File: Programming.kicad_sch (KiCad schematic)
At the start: 4 parts, among them J1 Programming Header, J2 Programming Jumper, SW4 EN

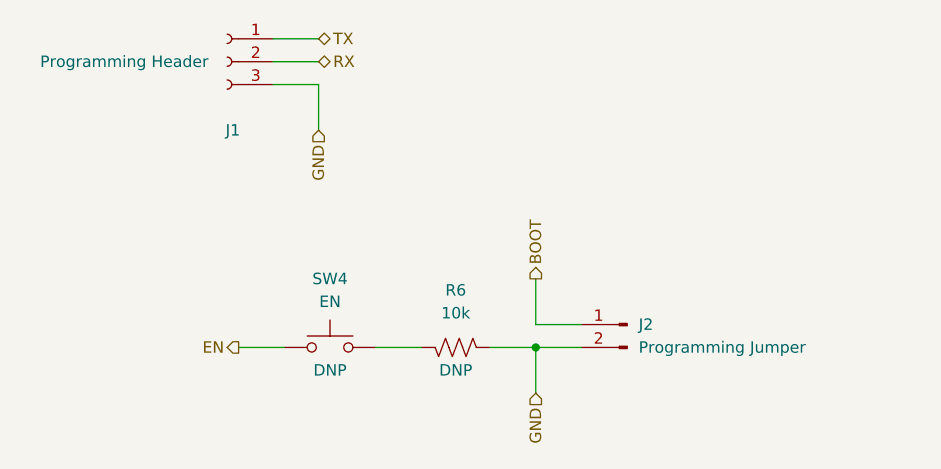
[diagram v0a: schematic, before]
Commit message: add ADC circuit, a few more DNP components, and assigned footprints
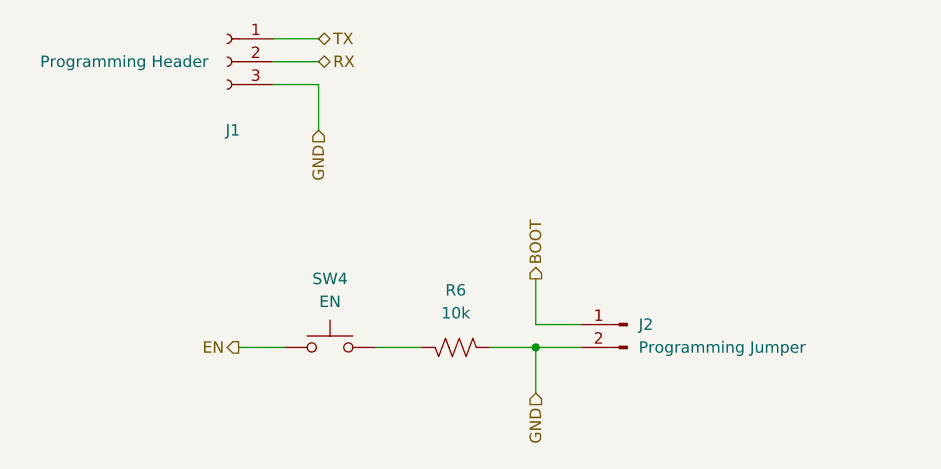
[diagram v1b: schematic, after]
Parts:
- J1: footprint (none) -> Connector_PinHeader_2.54mm:PinHeader_1x03_P2.54mm_Horizontal
- J2: footprint (none) -> Connector_PinHeader_2.54mm:PinHeader_1x02_P2.54mm_Horizontal
- R6: footprint (none) -> Resistor_SMD:R_0603_1608Metric; Field4 DNP -> (none)
- SW4: footprint (none) -> Button_Switch_SMD:SW_SPST_TL3305B; Field4 DNP -> (none)
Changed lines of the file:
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@@
       (effects (font (size 1.27 1.27)))
     )
-    (property "Footprint" "" (at 132.08 110.49 0)
+    (property "Footprint" "Button_Switch_SMD:SW_SPST_TL3305B" (at 132.08 110.49 0)
       (effects (font (size 1.27 1.27)) hide)
     )
     (property "Datasheet" "~" (at 132.08 110.49 0)
       (effects (font (size 1.27 1.27)) hide)
-    )
-    (property "Field4" "DNP" (at 132.08 118.11 0)
-      (effects (font (size 1.27 1.27)))
     )
     (pin "1")
@@
       (effects (font (size 1.27 1.27)))
     )
-    (property "Footprint" "" (at 120.65 83.82 0)
+    (property "Footprint" "Connector_PinHeader_2.54mm:PinHeader_1x03_P2.54mm_Horizontal" (at 120.65 83.82 0)
       (effects (font (size 1.27 1.27)) hide)
     )
@@
       (effects (font (size 1.27 1.27)))
     )
-    (property "Footprint" "" (at 146.304 116.586 90)
+    (property "Footprint" "Resistor_SMD:R_0603_1608Metric" (at 146.304 116.586 90)
       (effects (font (size 1.27 1.27)) hide)
     )
     (property "Datasheet" "~" (at 146.05 115.57 0)
       (effects (font (size 1.27 1.27)) hide)
-    )
-    (property "Field4" "DNP" (at 146.05 118.11 90)
-      (effects (font (size 1.27 1.27)))
     )
     (pin "1")
@@
         )
         (path "/b002c3bf-fc58-4993-80f7-7914d3aa1ac9/a04b704b-7ebc-4a7f-8071-91aed1728ce2"
-          (reference "R9") (unit 1)
+          (reference "R12") (unit 1)
         )
       )
@@
       (effects (font (size 1.27 1.27)) (justify right))
     )
-    (property "Footprint" "" (at 165.1 113.03 0)
+    (property "Footprint" "Connector_PinHeader_2.54mm:PinHeader_1x02_P2.54mm_Horizontal" (at 165.1 113.03 0)
       (effects (font (size 1.27 1.27)) hide)
     )

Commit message: inital layout of components complete
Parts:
- removed R6: 10k, Resistor_SMD:R_0603_1608Metric, symbol Device:R_US
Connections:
- net GND: now also SW4.1
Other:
- moved on the sheet: SW4
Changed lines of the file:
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@@
     (stroke (width 0) (type default))
   )
-  (wire (pts (xy 127 115.57) (xy 121.92 115.57))
+  (wire (pts (xy 139.7 115.57) (xy 134.62 115.57))
     (stroke (width 0) (type default))
   )
@@
     (stroke (width 0) (type default))
   )
-  (wire (pts (xy 137.16 115.57) (xy 142.24 115.57))
-    (stroke (width 0) (type default))
-  )
   (wire (pts (xy 154.94 107.95) (xy 154.94 113.03))
     (stroke (width 0) (type default))
   )
-  (hierarchical_label "EN" (shape output) (at 121.92 115.57 180) (fields_autoplaced)
+  (hierarchical_label "EN" (shape output) (at 134.62 115.57 180) (fields_autoplaced)
     (effects (font (size 1.27 1.27)) (justify right))
   )
@@
     (effects (font (size 1.27 1.27)) (justify left))
   )
-  (symbol (lib_id "Switch:SW_Push") (at 132.08 115.57 0) (mirror y) (unit 1)
+  (symbol (lib_id "Switch:SW_Push") (at 144.78 115.57 0) (mirror y) (unit 1)
     (in_bom yes) (on_board yes) (dnp no)
-    (property "Reference" "SW4" (at 132.08 107.95 0)
+    (property "Reference" "SW4" (at 144.78 107.95 0)
       (effects (font (size 1.27 1.27)))
     )
-    (property "Value" "EN" (at 132.08 110.49 0)
+    (property "Value" "EN" (at 144.78 110.49 0)
       (effects (font (size 1.27 1.27)))
     )
-    (property "Footprint" "Button_Switch_SMD:SW_SPST_TL3305B" (at 132.08 110.49 0)
+    (property "Footprint" "Button_Switch_SMD:SW_SPST_TL3305B" (at 144.78 110.49 0)
       (effects (font (size 1.27 1.27)) hide)
     )
-    (property "Datasheet" "~" (at 132.08 110.49 0)
+    (property "Datasheet" "~" (at 144.78 110.49 0)
       (effects (font (size 1.27 1.27)) hide)
     )
@@
         )
       )
-    )
-  )
-  (symbol (lib_id "Device:R_US") (at 146.05 115.57 90) (mirror x) (unit 1)
-    (in_bom yes) (on_board yes) (dnp no)
-    (property "Reference" "R6" (at 146.05 109.22 90)
-      (effects (font (size 1.27 1.27)))
-    )
-    (property "Value" "10k" (at 146.05 111.76 90)
-      (effects (font (size 1.27 1.27)))
-    )
-    (property "Footprint" "Resistor_SMD:R_0603_1608Metric" (at 146.304 116.586 90)
-      (effects (font (size 1.27 1.27)) hide)
-    )
-    (property "Datasheet" "~" (at 146.05 115.57 0)
-      (effects (font (size 1.27 1.27)) hide)
-    )
-    (pin "1")
-    (pin "2")
-    (instances
-      (project "key-fob-pcb"
-        (path "/b002c3bf-fc58-4993-80f7-7914d3aa1ac9/2e0921b6-f0d9-4f19-880e-02dc034cc8b0"
-          (reference "R6") (unit 1)
-        )
-        (path "/b002c3bf-fc58-4993-80f7-7914d3aa1ac9/a04b704b-7ebc-4a7f-8071-91aed1728ce2"
-          (reference "R12") (unit 1)
-        )
-      )

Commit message: layout complete
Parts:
- renumbered J2 to J1, J1 to J2
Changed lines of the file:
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@@
   (junction (at 154.94 115.57) (diameter 0) (color 0 0 0 0)
+  )
+  (wire (pts (xy 125.73 81.28) (xy 130.81 81.28))
+    (stroke (width 0) (type default))
   )
   (wire (pts (xy 125.73 86.36) (xy 130.81 86.36))
@@
     (stroke (width 0) (type default))
   )
-  (wire (pts (xy 125.73 81.28) (xy 130.81 81.28))
+  (wire (pts (xy 125.73 83.82) (xy 130.81 83.82))
     (stroke (width 0) (type default))
   )
@@
   )
   (wire (pts (xy 139.7 115.57) (xy 134.62 115.57))
-    (stroke (width 0) (type default))
-  )
-  (wire (pts (xy 125.73 83.82) (xy 130.81 83.82))
     (stroke (width 0) (type default))
   )
@@
         )
         (path "/b002c3bf-fc58-4993-80f7-7914d3aa1ac9/a04b704b-7ebc-4a7f-8071-91aed1728ce2"
-          (reference "SW5") (unit 1)
+          (reference "SW2") (unit 1)
         )
       )
@@
   (symbol (lib_id "Connector:Conn_01x03_Socket") (at 120.65 83.82 0) (mirror y) (unit 1)
     (in_bom yes) (on_board yes) (dnp no)
-    (property "Reference" "J1" (at 121.285 91.44 0)
+    (property "Reference" "J2" (at 121.285 91.44 0)
       (effects (font (size 1.27 1.27)))
     )
@@
       (project "key-fob-pcb"
         (path "/b002c3bf-fc58-4993-80f7-7914d3aa1ac9/a04b704b-7ebc-4a7f-8071-91aed1728ce2"
-          (reference "J1") (unit 1)
+          (reference "J2") (unit 1)
         )
       )
@@
   (symbol (lib_id "Connector:Conn_01x02_Pin") (at 165.1 113.03 0) (mirror y) (unit 1)
     (in_bom yes) (on_board yes) (dnp no) (fields_autoplaced)
-    (property "Reference" "J2" (at 166.37 113.03 0)
+    (property "Reference" "J1" (at 166.37 113.03 0)
       (effects (font (size 1.27 1.27)) (justify right))
     )
@@
       (project "key-fob-pcb"
         (path "/b002c3bf-fc58-4993-80f7-7914d3aa1ac9/a04b704b-7ebc-4a7f-8071-91aed1728ce2"
-          (reference "J2") (unit 1)
+          (reference "J1") (unit 1)
         )
       )

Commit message: generate fab files
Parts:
- J1, J2, SW4: now left out of the parts list
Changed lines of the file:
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@@
   )
   (symbol (lib_id "Switch:SW_Push") (at 144.78 115.57 0) (mirror y) (unit 1)
-    (in_bom yes) (on_board yes) (dnp no)
+    (in_bom no) (on_board yes) (dnp no)
     (property "Reference" "SW4" (at 144.78 107.95 0)
       (effects (font (size 1.27 1.27)))
@@
   )
   (symbol (lib_id "Connector:Conn_01x03_Socket") (at 120.65 83.82 0) (mirror y) (unit 1)
-    (in_bom yes) (on_board yes) (dnp no)
+    (in_bom no) (on_board yes) (dnp no)
     (property "Reference" "J2" (at 121.285 91.44 0)
       (effects (font (size 1.27 1.27)))
@@
   )
   (symbol (lib_id "Connector:Conn_01x02_Pin") (at 165.1 113.03 0) (mirror y) (unit 1)
-    (in_bom yes) (on_board yes) (dnp no) (fields_autoplaced)
+    (in_bom no) (on_board yes) (dnp no) (fields_autoplaced)
     (property "Reference" "J1" (at 166.37 113.03 0)
       (effects (font (size 1.27 1.27)) (justify right))

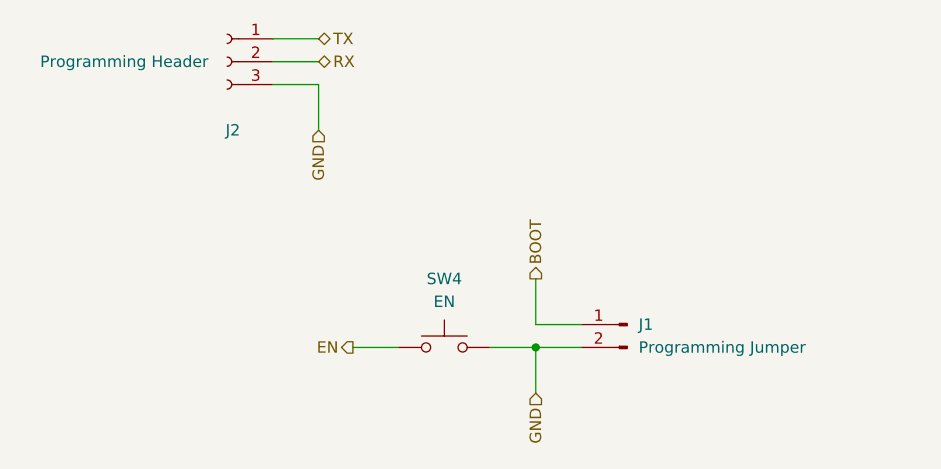
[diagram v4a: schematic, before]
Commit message: replace GND heriarchical labels with GND symbols
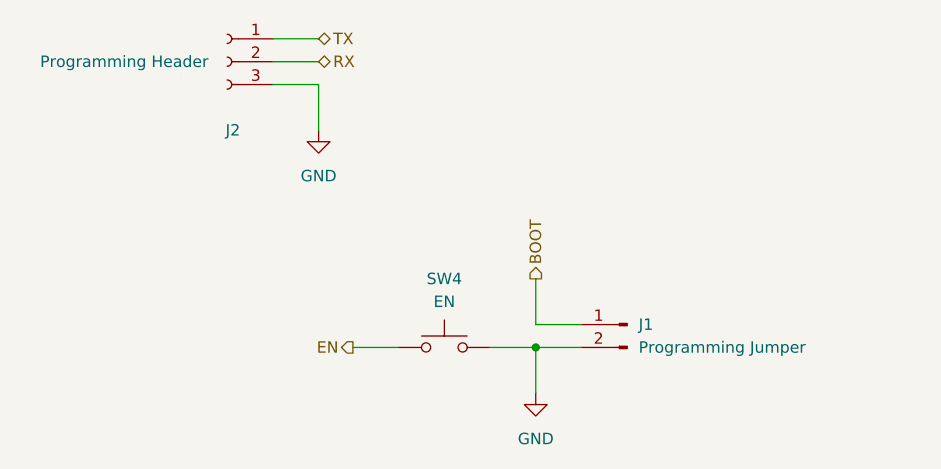
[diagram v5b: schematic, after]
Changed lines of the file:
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@@
     (effects (font (size 1.27 1.27)) (justify left))
-  )
-  (hierarchical_label "GND" (shape input) (at 130.81 91.44 270) (fields_autoplaced)
-    (effects (font (size 1.27 1.27)) (justify right))
-  )
-  (hierarchical_label "GND" (shape input) (at 154.94 120.65 270) (fields_autoplaced)
-    (effects (font (size 1.27 1.27)) (justify right))
   )
   (hierarchical_label "TX" (shape bidirectional) (at 130.81 81.28 0) (fields_autoplaced)
@@
         )
       )
+    )
+  )
+  (symbol (lib_id "power:GND") (at 130.81 91.44 0) (unit 1)
+    (in_bom yes) (on_board yes) (dnp no) (fields_autoplaced)
+    (property "Reference" "#PWR02" (at 130.81 97.79 0)
+      (effects (font (size 1.27 1.27)) hide)
+    )
+    (property "Value" "GND" (at 130.81 96.52 0)
+      (effects (font (size 1.27 1.27)))
+    )
+    (property "Footprint" "" (at 130.81 91.44 0)
+      (effects (font (size 1.27 1.27)) hide)
+    )
+    (property "Datasheet" "" (at 130.81 91.44 0)
+      (effects (font (size 1.27 1.27)) hide)
+    )
+    (pin "1")
+    (instances
+      (project "key-fob-pcb"
+        (path "/b002c3bf-fc58-4993-80f7-7914d3aa1ac9/97ab50b4-0765-4242-8cdd-feb1ed8d7056"
+          (reference "#PWR02") (unit 1)
+        )
+        (path "/b002c3bf-fc58-4993-80f7-7914d3aa1ac9/a04b704b-7ebc-4a7f-8071-91aed1728ce2"
+          (reference "#PWR08") (unit 1)
+        )
+      )
+    )
+  )
+  (symbol (lib_id "power:GND") (at 154.94 120.65 0) (unit 1)
+    (in_bom yes) (on_board yes) (dnp no) (fields_autoplaced)
+    (property "Reference" "#PWR07" (at 154.94 127 0)
+      (effects (font (size 1.27 1.27)) hide)
+    )
+    (property "Value" "GND" (at 154.94 125.73 0)
+      (effects (font (size 1.27 1.27)))
+    )
+    (property "Footprint" "" (at 154.94 120.65 0)
+      (effects (font (size 1.27 1.27)) hide)
+    )
+    (property "Datasheet" "" (at 154.94 120.65 0)
+      (effects (font (size 1.27 1.27)) hide)
+    )
+    (pin "1")
+    (instances
+      (project "key-fob-pcb"
+        (path "/b002c3bf-fc58-4993-80f7-7914d3aa1ac9/a04b704b-7ebc-4a7f-8071-91aed1728ce2"
+          (reference "#PWR07") (unit 1)
+        )
+      )

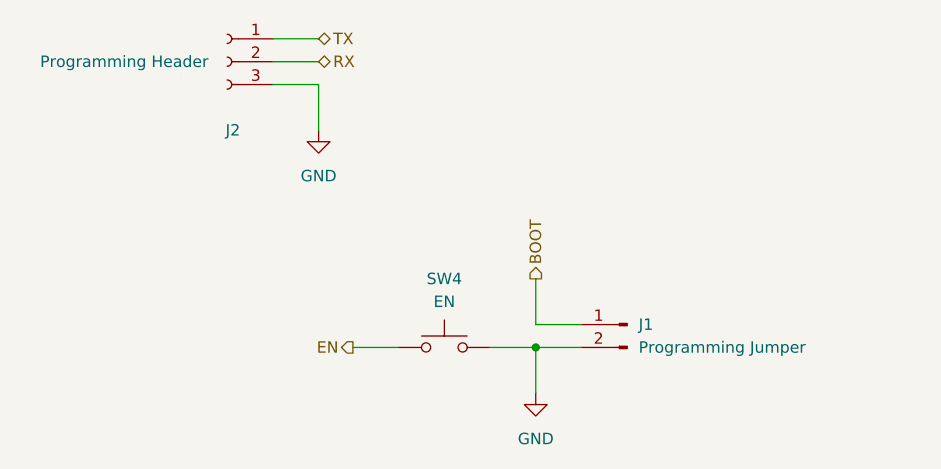
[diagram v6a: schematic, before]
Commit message: switched to full-sized ESP32 S3 WROOM and redid PCB layout
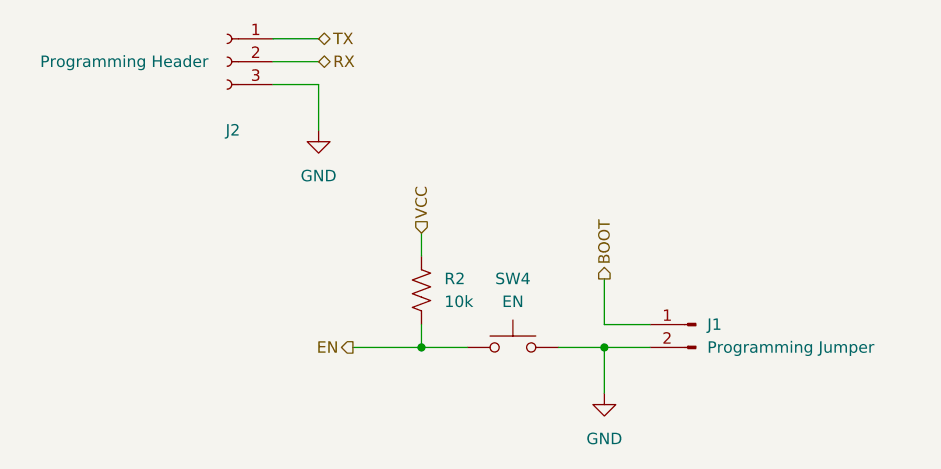
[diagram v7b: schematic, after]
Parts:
- added R2: 10k, Resistor_SMD:R_0603_1608Metric, symbol Device:R_US
- J1: footprint Connector_PinHeader_2.54mm:PinHeader_1x02_P2.54mm_Horizontal -> SAMTEC_TSM-102-01-L-SH:SAMTEC_TSM-102-01-L-SH
- J2: footprint Connector_PinHeader_2.54mm:PinHeader_1x03_P2.54mm_Horizontal -> SAMTEC_TSM-103-01-L-SH-TR:SAMTEC_TSM-103-01-L-SH-TR
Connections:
- net EN: now also R2.2
- new net VCC: R2.1
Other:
- moved on the sheet: J1, SW4
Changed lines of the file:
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@@
     (comment 1 "Author: Ben Martens")
   )
-  (junction (at 154.94 115.57) (diameter 0) (color 0 0 0 0)
+  (junction (at 162.56 115.57) (diameter 0) (color 0 0 0 0)
+  )
+  (junction (at 142.24 115.57) (diameter 0) (color 0 0 0 0)
   )
   (wire (pts (xy 125.73 81.28) (xy 130.81 81.28))
@@
     (stroke (width 0) (type default))
   )
+  (wire (pts (xy 142.24 113.03) (xy 142.24 115.57))
+    (stroke (width 0) (type default))
+  )
   (wire (pts (xy 130.81 86.36) (xy 130.81 91.44))
     (stroke (width 0) (type default))
   )
-  (wire (pts (xy 149.86 115.57) (xy 154.94 115.57))
-    (stroke (width 0) (type default))
-  )
-  (wire (pts (xy 154.94 115.57) (xy 154.94 120.65))
+  (wire (pts (xy 142.24 102.87) (xy 142.24 105.41))
+    (stroke (width 0) (type default))
+  )
+  (wire (pts (xy 157.48 115.57) (xy 162.56 115.57))
+    (stroke (width 0) (type default))
+  )
+  (wire (pts (xy 162.56 115.57) (xy 162.56 120.65))
     (stroke (width 0) (type default))
   )
@@
     (stroke (width 0) (type default))
   )
-  (wire (pts (xy 154.94 113.03) (xy 160.02 113.03))
-    (stroke (width 0) (type default))
-  )
-  (wire (pts (xy 139.7 115.57) (xy 134.62 115.57))
-    (stroke (width 0) (type default))
-  )
-  (wire (pts (xy 160.02 115.57) (xy 154.94 115.57))
-    (stroke (width 0) (type default))
-  )
-  (wire (pts (xy 154.94 107.95) (xy 154.94 113.03))
+  (wire (pts (xy 162.56 113.03) (xy 167.64 113.03))
+    (stroke (width 0) (type default))
+  )
+  (wire (pts (xy 142.24 115.57) (xy 134.62 115.57))
+    (stroke (width 0) (type default))
+  )
+  (wire (pts (xy 147.32 115.57) (xy 142.24 115.57))
+    (stroke (width 0) (type default))
+  )
+  (wire (pts (xy 167.64 115.57) (xy 162.56 115.57))
+    (stroke (width 0) (type default))
+  )
+  (wire (pts (xy 162.56 107.95) (xy 162.56 113.03))
     (stroke (width 0) (type default))
   )
@@
     (effects (font (size 1.27 1.27)) (justify right))
   )
-  (hierarchical_label "BOOT" (shape output) (at 154.94 107.95 90) (fields_autoplaced)
+  (hierarchical_label "BOOT" (shape output) (at 162.56 107.95 90) (fields_autoplaced)
     (effects (font (size 1.27 1.27)) (justify left))
   )
@@
     (effects (font (size 1.27 1.27)) (justify left))
   )
+  (hierarchical_label "VCC" (shape input) (at 142.24 102.87 90) (fields_autoplaced)
+    (effects (font (size 1.27 1.27)) (justify left))
+  )
   (hierarchical_label "RX" (shape bidirectional) (at 130.81 83.82 0) (fields_autoplaced)
     (effects (font (size 1.27 1.27)) (justify left))
   )
-  (symbol (lib_id "Switch:SW_Push") (at 144.78 115.57 0) (mirror y) (unit 1)
+  (symbol (lib_id "Switch:SW_Push") (at 152.4 115.57 0) (mirror y) (unit 1)
     (in_bom no) (on_board yes) (dnp no)
-    (property "Reference" "SW4" (at 144.78 107.95 0)
-      (effects (font (size 1.27 1.27)))
-    )
-    (property "Value" "EN" (at 144.78 110.49 0)
-      (effects (font (size 1.27 1.27)))
-    )
-    (property "Footprint" "Button_Switch_SMD:SW_SPST_TL3305B" (at 144.78 110.49 0)
-      (effects (font (size 1.27 1.27)) hide)
-    )
-    (property "Datasheet" "~" (at 144.78 110.49 0)
+    (property "Reference" "SW4" (at 152.4 107.95 0)
+      (effects (font (size 1.27 1.27)))
+    )
+    (property "Value" "EN" (at 152.4 110.49 0)
+      (effects (font (size 1.27 1.27)))
+    )
+    (property "Footprint" "Button_Switch_SMD:SW_SPST_TL3305B" (at 152.4 110.49 0)
+      (effects (font (size 1.27 1.27)) hide)
+    )
+    (property "Datasheet" "~" (at 152.4 110.49 0)
       (effects (font (size 1.27 1.27)) hide)
     )
@@
       (effects (font (size 1.27 1.27)))
     )
-    (property "Footprint" "Connector_PinHeader_2.54mm:PinHeader_1x03_P2.54mm_Horizontal" (at 120.65 83.82 0)
+    (property "Footprint" "SAMTEC_TSM-103-01-L-SH-TR:SAMTEC_TSM-103-01-L-SH-TR" (at 120.65 83.82 0)
       (effects (font (size 1.27 1.27)) hide)
     )
@@
     )
   )
-  (symbol (lib_id "Connector:Conn_01x02_Pin") (at 165.1 113.03 0) (mirror y) (unit 1)
+  (symbol (lib_id "Connector:Conn_01x02_Pin") (at 172.72 113.03 0) (mirror y) (unit 1)
     (in_bom no) (on_board yes) (dnp no) (fields_autoplaced)
-    (property "Reference" "J1" (at 166.37 113.03 0)
+    (property "Reference" "J1" (at 173.99 113.03 0)
       (effects (font (size 1.27 1.27)) (justify right))
     )
-    (property "Value" "Programming Jumper" (at 166.37 115.57 0)
+    (property "Value" "Programming Jumper" (at 173.99 115.57 0)
       (effects (font (size 1.27 1.27)) (justify right))
     )
-    (property "Footprint" "Connector_PinHeader_2.54mm:PinHeader_1x02_P2.54mm_Horizontal" (at 165.1 113.03 0)
-      (effects (font (size 1.27 1.27)) hide)
-    )
-    (property "Datasheet" "~" (at 165.1 113.03 0)
+    (property "Footprint" "SAMTEC_TSM-102-01-L-SH:SAMTEC_TSM-102-01-L-SH" (at 172.72 113.03 0)
+      (effects (font (size 1.27 1.27)) hide)
+    )
+    (property "Datasheet" "~" (at 172.72 113.03 0)
       (effects (font (size 1.27 1.27)) hide)
     )
@@
     )
   )
-  (symbol (lib_id "power:GND") (at 154.94 120.65 0) (unit 1)
+  (symbol (lib_id "Device:R_US") (at 142.24 109.22 0) (unit 1)
     (in_bom yes) (on_board yes) (dnp no) (fields_autoplaced)
-    (property "Reference" "#PWR07" (at 154.94 127 0)
-      (effects (font (size 1.27 1.27)) hide)
-    )
-    (property "Value" "GND" (at 154.94 125.73 0)
-      (effects (font (size 1.27 1.27)))
-    )
-    (property "Footprint" "" (at 154.94 120.65 0)
-      (effects (font (size 1.27 1.27)) hide)
-    )
-    (property "Datasheet" "" (at 154.94 120.65 0)
-      (effects (font (size 1.27 1.27)) hide)
-    )
+    (property "Reference" "R2" (at 144.78 107.95 0)
+      (effects (font (size 1.27 1.27)) (justify left))
+    )
+    (property "Value" "10k" (at 144.78 110.49 0)
+      (effects (font (size 1.27 1.27)) (justify left))
+    )
+    (property "Footprint" "Resistor_SMD:R_0603_1608Metric" (at 143.256 109.474 90)
+      (effects (font (size 1.27 1.27)) hide)
+    )
+    (property "Datasheet" "~" (at 142.24 109.22 0)
+      (effects (font (size 1.27 1.27)) hide)
+    )
+    (pin "1")
+    (pin "2")
+    (instances
+      (project "control-module-pcb"
+        (path "/4c946e98-79c2-4a2d-bd7f-2a33db8d8c91/689f1063-70bb-4257-9aa2-434555b9eee7"
+          (reference "R2") (unit 1)
+        )
+      )
+      (project "key-fob-pcb"
+        (path "/b002c3bf-fc58-4993-80f7-7914d3aa1ac9/a04b704b-7ebc-4a7f-8071-91aed1728ce2"
+          (reference "R2") (unit 1)
+        )
+      )
+    )
+  )
+  (symbol (lib_id "power:GND") (at 162.56 120.65 0) (unit 1)
+    (in_bom yes) (on_board yes) (dnp no) (fields_autoplaced)
+    (property "Reference" "#PWR07" (at 162.56 127 0)
+      (effects (font (size 1.27 1.27)) hide)
+    )
+    (property "Value" "GND" (at 162.56 125.73 0)
+      (effects (font (size 1.27 1.27)))
+    )
+    (property "Footprint" "" (at 162.56 120.65 0)
+      (effects (font (size 1.27 1.27)) hide)
+    )
+    (property "Datasheet" "" (at 162.56 120.65 0)
+      (effects (font (size 1.27 1.27)) hide)
+    )
